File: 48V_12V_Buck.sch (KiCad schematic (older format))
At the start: 8 parts

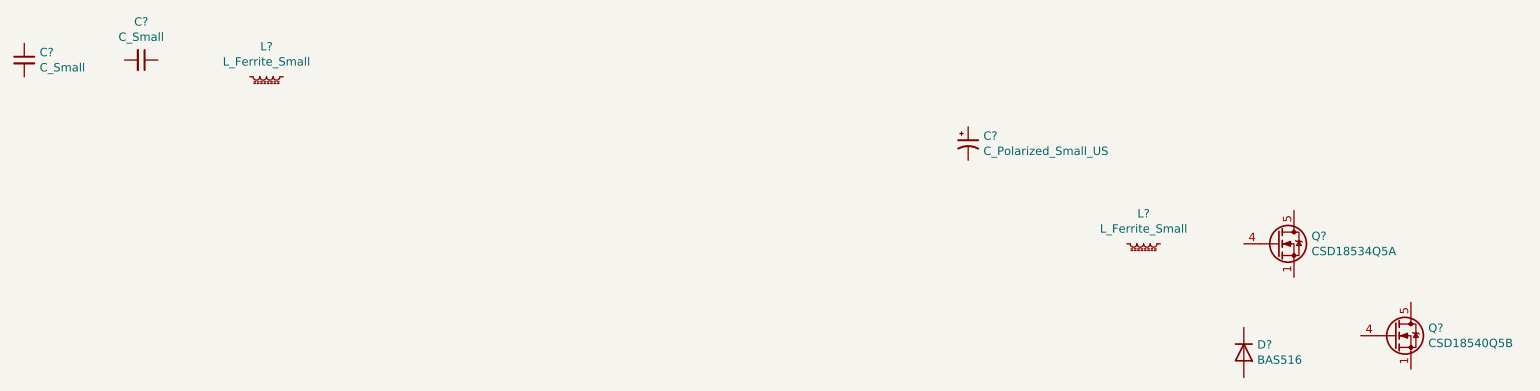
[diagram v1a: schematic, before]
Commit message: Added USB SRAM sheet,Added USB3 ethernet ic
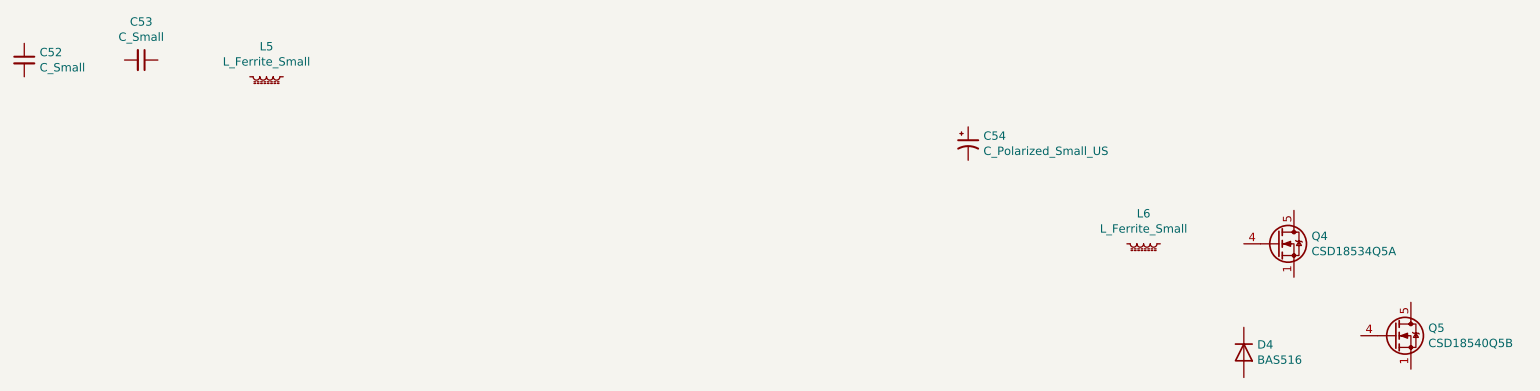
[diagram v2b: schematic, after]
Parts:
- gave numbers to parts that had none: 8
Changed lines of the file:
@@
 $Descr A4 11693 8268
 encoding utf-8
-Sheet 14 15
+Sheet 17 17
 Title ""
 Date ""
@@
 $EndDescr
 $Comp
-L Device:C_Small C?
+L Device:C_Small C52
 U 1 1 60264835
 P 1950 750
-F 0 "C?" H 2042 796 50  0000 L CNN
+F 0 "C52" H 2042 796 50  0000 L CNN
 F 1 "C_Small" H 2042 705 50  0000 L CNN
 F 2 "" H 1950 750 50  0001 C CNN
@@
 $EndComp
 $Comp
-L Device:C_Small C?
+L Device:C_Small C53
 U 1 1 60264F4A
 P 2650 750
-F 0 "C?" V 2421 750 50  0000 C CNN
+F 0 "C53" V 2421 750 50  0000 C CNN
 F 1 "C_Small" V 2512 750 50  0000 C CNN
 F 2 "" H 2650 750 50  0001 C CNN
@@
 $EndComp
 $Comp
-L Device:L_Ferrite_Small L?
+L Device:L_Ferrite_Small L5
 U 1 1 602665A9
 P 3400 850
-F 0 "L?" V 3219 850 50  0000 C CNN
+F 0 "L5" V 3219 850 50  0000 C CNN
 F 1 "L_Ferrite_Small" V 3310 850 50  0000 C CNN
 F 2 "" H 3400 850 50  0001 C CNN
@@
 $EndComp
 $Comp
-L Device:L_Ferrite_Small L?
+L Device:L_Ferrite_Small L6
 U 1 1 6026814B
 P 8650 1850
-F 0 "L?" V 8469 1850 50  0000 C CNN
+F 0 "L6" V 8469 1850 50  0000 C CNN
 F 1 "L_Ferrite_Small" V 8560 1850 50  0000 C CNN
 F 2 "" H 8650 1850 50  0001 C CNN
@@
 $EndComp
 $Comp
-L Transistor_FET:CSD18534Q5A Q?
+L Transistor_FET:CSD18534Q5A Q4
 U 1 1 60269229
 P 9450 1850
-F 0 "Q?" H 9655 1896 50  0000 L CNN
+F 0 "Q4" H 9655 1896 50  0000 L CNN
 F 1 "CSD18534Q5A" H 9655 1805 50  0000 L CNN
 F 2 "Package_TO_SOT_SMD:TDSON-8-1" H 9650 1775 50  0001 L CIN
@@
 $EndComp
 $Comp
-L Diode:BAS516 D?
+L Diode:BAS516 D4
 U 1 1 6026AF6B
 P 9250 2500
-F 0 "D?" V 9204 2580 50  0000 L CNN
+F 0 "D4" V 9204 2580 50  0000 L CNN
 F 1 "BAS516" V 9295 2580 50  0000 L CNN
 F 2 "Diode_SMD:D_SOD-523" H 9250 2325 50  0001 C CNN
@@
 $EndComp
 $Comp
-L Transistor_FET:CSD18540Q5B Q?
+L Transistor_FET:CSD18540Q5B Q5
 U 1 1 6026C128
 P 10150 2400
-F 0 "Q?" H 10354 2446 50  0000 L CNN
+F 0 "Q5" H 10354 2446 50  0000 L CNN
 F 1 "CSD18540Q5B" H 10354 2355 50  0000 L CNN
 F 2 "Package_TO_SOT_SMD:TDSON-8-1" H 10350 2325 50  0001 L CIN
@@
 $EndComp
 $Comp
-L Device:C_Polarized_Small_US C?
+L Device:C_Polarized_Small_US C54
 U 1 1 60271F7C
 P 7600 1250
-F 0 "C?" H 7691 1296 50  0000 L CNN
+F 0 "C54" H 7691 1296 50  0000 L CNN
 F 1 "C_Polarized_Small_US" H 7691 1205 50  0000 L CNN
 F 2 "Capacitor_SMD:CP_Elec_6.3x5.9" H 7600 1250 50  0001 C CNN

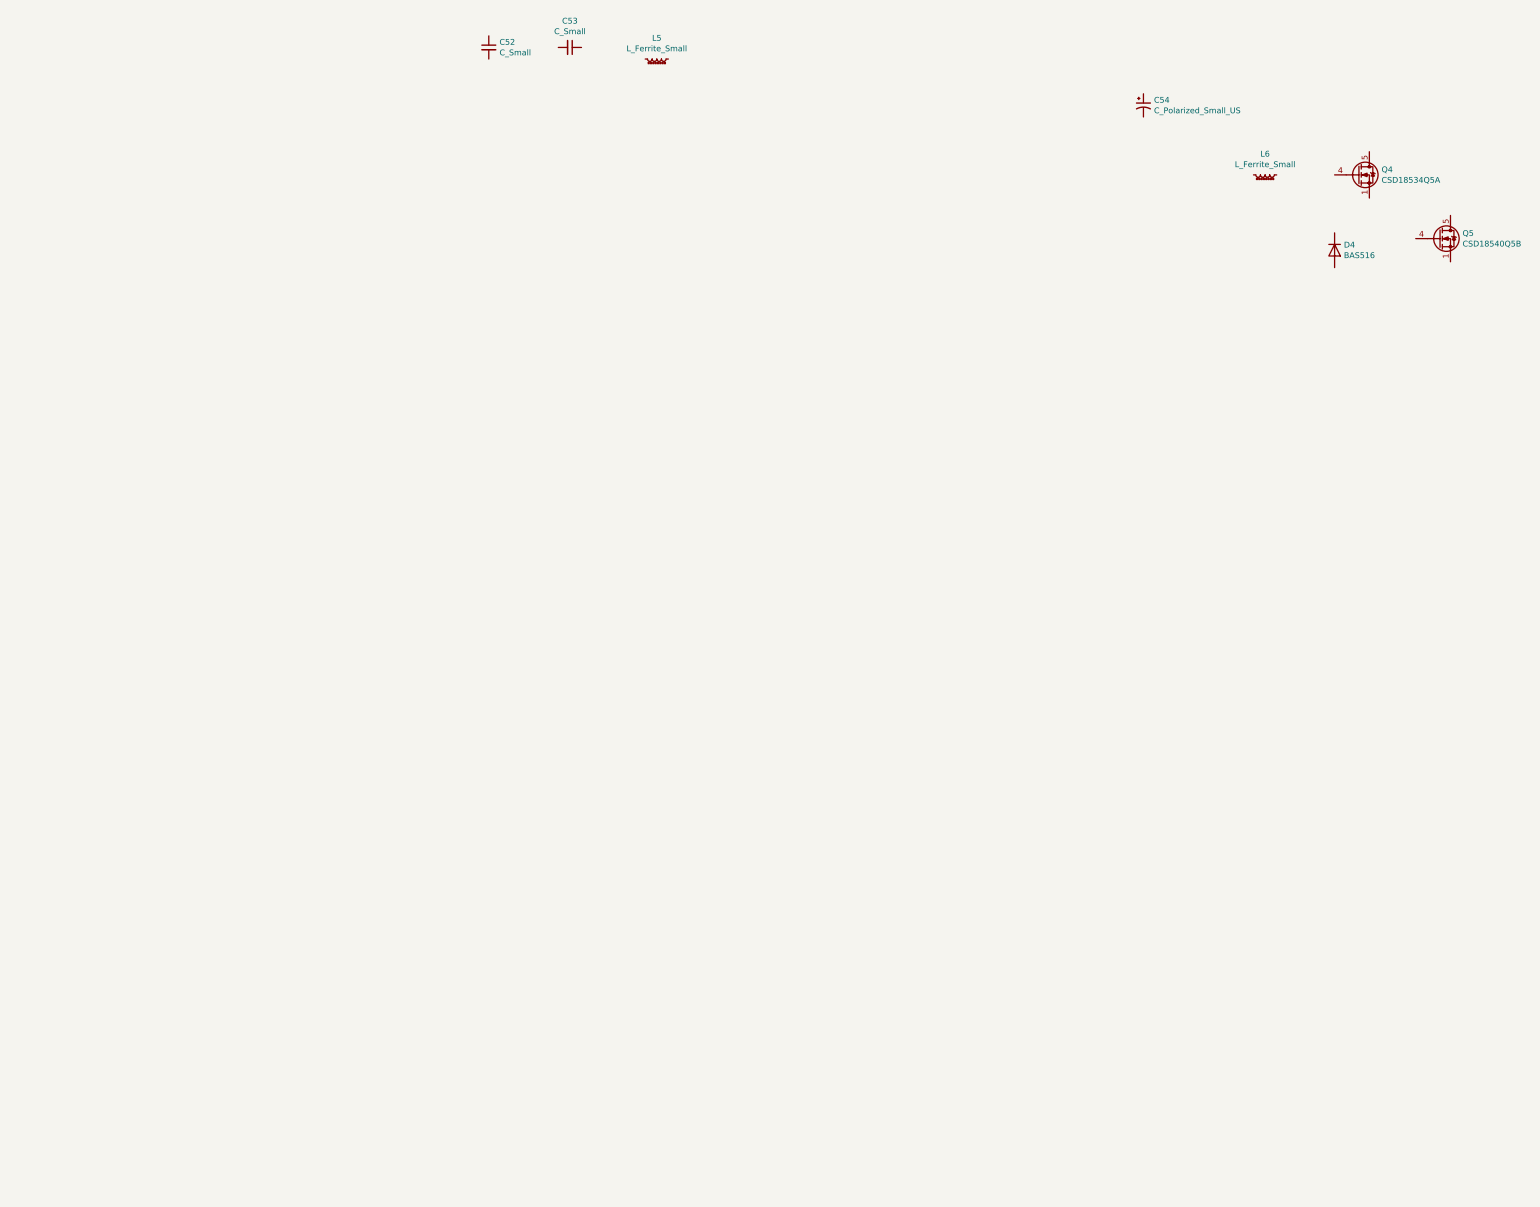
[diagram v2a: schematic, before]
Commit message: Completed power 48v to 12v sheet
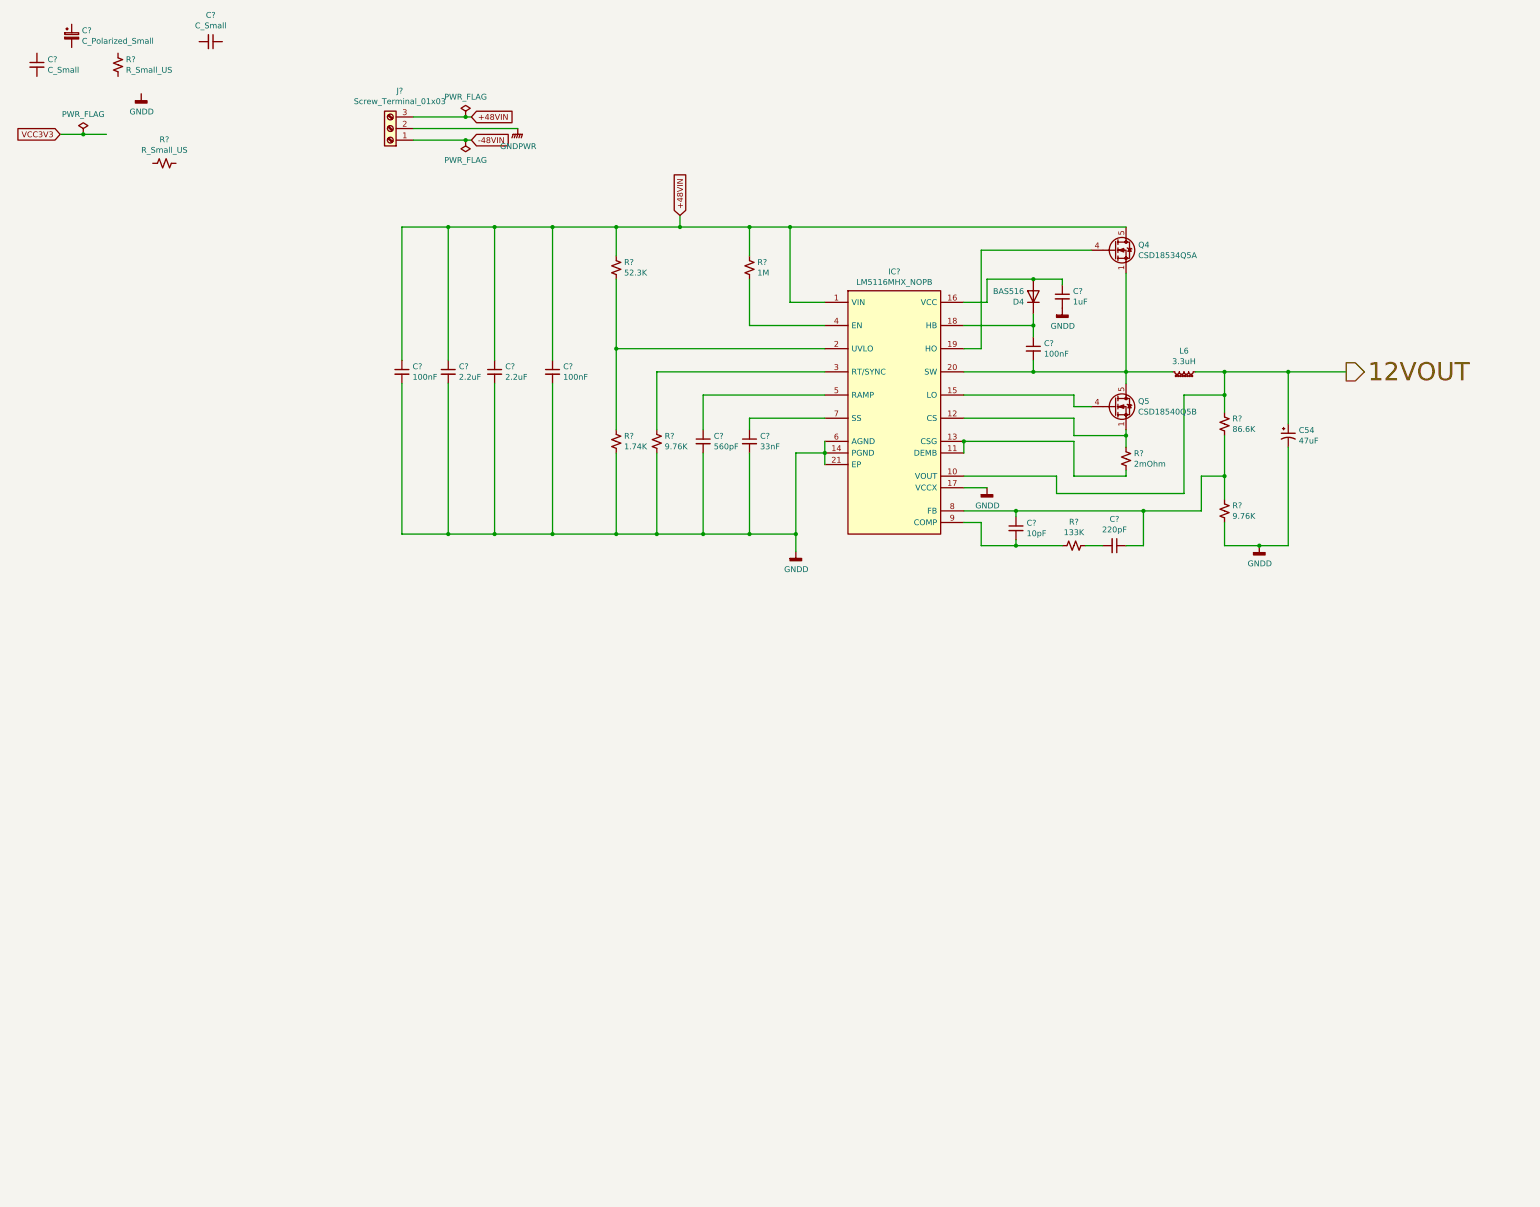
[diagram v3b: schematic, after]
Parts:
- removed C52, C53: C_Small, symbol Device:C_Small
- removed L5: L_Ferrite_Small, symbol Device:L_Ferrite_Small
- added C?: C_Small, Capacitor_SMD:C_0603_1608Metric_Pad1.08x0.95mm_HandSolder, symbol Device:C_Small
- added C?: C_Polarized_Small, Capacitor_Tantalum_SMD:CP_EIA-1608-10_AVX-L_Pad1.25x1.05mm_HandSolder, symbol Device:C_Polarized_Small
- added C?: C_Small, symbol Device:C_Small
- added C?: 33nF, Capacitor_SMD:C_0603_1608Metric_Pad1.08x0.95mm_HandSolder, symbol Device:C_Small
- added C?: 560pF, Capacitor_SMD:C_0603_1608Metric_Pad1.08x0.95mm_HandSolder, symbol Device:C_Small
- added C? (x3): 100nF, Capacitor_SMD:C_0603_1608Metric_Pad1.08x0.95mm_HandSolder, symbol Device:C_Small
- added C? (x2): 2.2uF, Capacitor_SMD:C_0603_1608Metric_Pad1.08x0.95mm_HandSolder, symbol Device:C_Small
- added C?: 1uF, Capacitor_SMD:C_0603_1608Metric_Pad1.08x0.95mm_HandSolder, symbol Device:C_Small
- added C?: 10pF, Capacitor_SMD:C_0603_1608Metric_Pad1.08x0.95mm_HandSolder, symbol Device:C_Small
- added C?: 220pF, Capacitor_SMD:C_0603_1608Metric_Pad1.08x0.95mm_HandSolder, symbol Device:C_Small
- added IC?: LM5116MHX_NOPB, SOP65P640X110-21N, symbol GM_Voltage_Regulators:LM5116MHX_NOPB
- added J?: Screw_Terminal_01x03, TerminalBlock:TerminalBlock_Altech_AK300-3_P5.00mm, symbol Connector:Screw_Terminal_01x03
- added R? (x2): R_Small_US, Resistor_SMD:R_0603_1608Metric_Pad0.98x0.95mm_HandSolder, symbol Device:R_Small_US
- added R?: 1M, Resistor_SMD:R_0603_1608Metric_Pad0.98x0.95mm_HandSolder, symbol Device:R_Small_US
- added R?: 52.3K, Resistor_SMD:R_0603_1608Metric_Pad0.98x0.95mm_HandSolder, symbol Device:R_Small_US
- added R?: 1.74K, Resistor_SMD:R_0603_1608Metric_Pad0.98x0.95mm_HandSolder, symbol Device:R_Small_US
- added R? (x2): 9.76K, Resistor_SMD:R_0603_1608Metric_Pad0.98x0.95mm_HandSolder, symbol Device:R_Small_US
- added R?: 2mOhm, Resistor_SMD:R_0603_1608Metric_Pad0.98x0.95mm_HandSolder, symbol Device:R_Small_US
- added R?: 133K, Resistor_SMD:R_0603_1608Metric_Pad0.98x0.95mm_HandSolder, symbol Device:R_Small_US
- added R?: 86.6K, Resistor_SMD:R_0603_1608Metric_Pad0.98x0.95mm_HandSolder, symbol Device:R_Small_US
- C54: value C_Polarized_Small_US -> 47uF
- L6: value L_Ferrite_Small -> 3.3uH; footprint (none) -> GM_Inductors:IHLP6767GZER3R3M01; MPN (none) -> IHLP6767GZER3R3M01
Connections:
- net 12VOUT: now reaches L6.1
- net 12VOUT: now also C54.1, IC?.10 (VOUT), R?.1
- net at L6.2: now also Q4.1 (S), Q4.2 (S), Q4.3 (S), Q5.5 (D), C?.2, IC?.20 (SW)
- net at Q4.4 (G): now also IC?.19 (HO)
- net +48VIN: now reaches Q4.5 (D)
- net +48VIN: now also C?.1, C?.1, C?.1, C?.1, IC?.1 (VIN), J?.3 (Pin_3), R?.1, R?.1
- net at D4.1 (K): now also C?.1, IC?.18 (HB)
- net at D4.2 (A): now also C?.1, IC?.16 (VCC)
- net at Q5.1 (S), Q5.2 (S), Q5.3 (S): now also IC?.12 (CS), R?.1
- net at Q5.4 (G): now also IC?.15 (LO)
- net GNDD: now reaches C54.2
- net GNDD: now also C?.2, C?.2, C?.2, C?.2, C?.2, C?.2, C?.2, IC?.14 (PGND), IC?.17 (VCCX), IC?.21 (EP), IC?.6 (AGND), R?.2, R?.2, R?.2
- new net: IC?.11 (DEMB), IC?.13 (CSG), R?.2
- new net: IC?.2 (UVLO), R?.1, R?.2
- new net: IC?.3 (RT/SYNC), R?.1
- new net: IC?.4 (EN), R?.2
- new net: C?.1, IC?.5 (RAMP)
- new net: C?.1, IC?.7 (SS)
- new net: C?.1, C?.1, IC?.8 (FB), R?.1, R?.2
- new net: C?.2, IC?.9 (COMP), R?.2
- new net: C?.2, R?.1
- new net -48VIN: J?.1 (Pin_1)
- new net GNDPWR: J?.2 (Pin_2)
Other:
- moved on the sheet: C54, D4, L6, Q4, Q5
